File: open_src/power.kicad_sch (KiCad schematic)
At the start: 9 parts

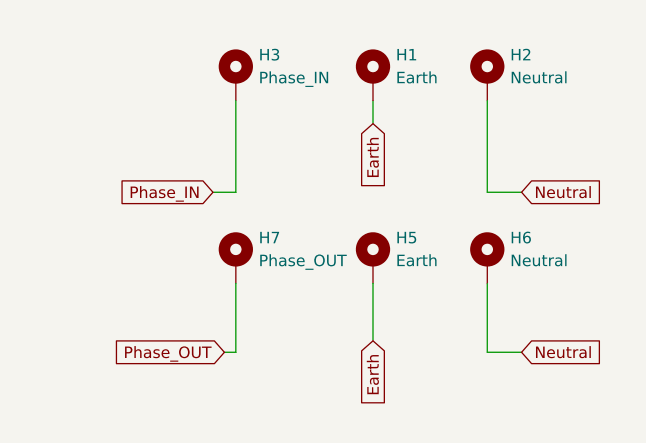
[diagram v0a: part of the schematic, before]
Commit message: Added trace
Still not yet cross checked
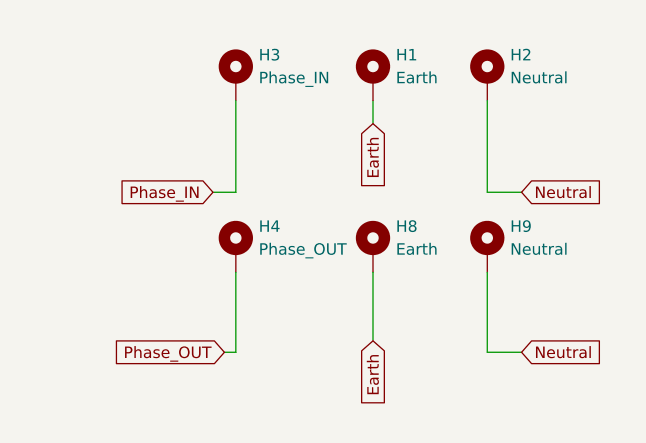
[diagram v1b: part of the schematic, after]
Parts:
- removed H5: Earth, Mounting_Wuerth:Mounting_Wuerth_WA-SMSE-ExternalM3_H8mm_9771080360, symbol Mechanical:MountingHole_Pad_MP
- removed H6: Neutral, Mounting_Wuerth:Mounting_Wuerth_WA-SMSE-ExternalM3_H5mm_9771050360, symbol Mechanical:MountingHole_Pad_MP
- removed H7: Phase_OUT, Mounting_Wuerth:Mounting_Wuerth_WA-SMSE-ExternalM3_H5mm_9771050360, symbol Mechanical:MountingHole_Pad_MP
- added H4: Phase_OUT, MountingHole:MountingHole_8.4mm_M8_Pad, symbol Mechanical:MountingHole_Pad
- added H8: Earth, MountingHole:MountingHole_8.4mm_M8_Pad, symbol Mechanical:MountingHole_Pad
- added H9: Neutral, MountingHole:MountingHole_8.4mm_M8_Pad, symbol Mechanical:MountingHole_Pad
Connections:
- net Earth: now also H8.1
- net Neutral: now also H9.1
- net Phase_OUT: now also H4.1
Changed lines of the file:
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@@
     (stroke (width 0) (type default))
   )
-  (wire (pts (xy 213.36 100.33) (xy 213.36 107.95))
+  (wire (pts (xy 213.36 99.06) (xy 213.36 107.95))
     (stroke (width 0) (type default))
   )
@@
     (stroke (width 0) (type default))
   )
-  (wire (pts (xy 228.6 100.33) (xy 228.6 106.68))
+  (wire (pts (xy 228.6 99.06) (xy 228.6 106.68))
     (stroke (width 0) (type default))
   )
@@
     (stroke (width 0) (type default))
   )
-  (wire (pts (xy 241.3 100.33) (xy 241.3 107.95))
+  (wire (pts (xy 241.3 99.06) (xy 241.3 107.95))
     (stroke (width 0) (type default))
   )
@@
     )
   )
+  (symbol (lib_id "Mechanical:MountingHole_Pad") (at 213.36 96.52 0) (unit 1)
+    (in_bom yes) (on_board yes) (dnp no) (fields_autoplaced)
+    (property "Reference" "H4" (at 215.9 93.98 0)
+      (effects (font (size 1.27 1.27)) (justify left))
+    )
+    (property "Value" "Phase_OUT" (at 215.9 96.52 0)
+      (effects (font (size 1.27 1.27)) (justify left))
+    )
+    (property "Footprint" "MountingHole:MountingHole_8.4mm_M8_Pad" (at 213.36 96.52 0)
+      (effects (font (size 1.27 1.27)) hide)
+    )
+    (property "Datasheet" "~" (at 213.36 96.52 0)
+      (effects (font (size 1.27 1.27)) hide)
+    )
+    (pin "1")
+    (instances
+      (project "open_src"
+        (path "/0eec0a72-c8ab-4737-8598-de474fd425a5/a922efa4-6ed1-4252-b0de-28fa44c32c4a"
+          (reference "H4") (unit 1)
+        )
+      )
+    )
+  )
+  (symbol (lib_id "Mechanical:MountingHole_Pad") (at 228.6 96.52 0) (unit 1)
+    (in_bom yes) (on_board yes) (dnp no) (fields_autoplaced)
+    (property "Reference" "H8" (at 231.14 93.98 0)
+      (effects (font (size 1.27 1.27)) (justify left))
+    )
+    (property "Value" "Earth" (at 231.14 96.52 0)
+      (effects (font (size 1.27 1.27)) (justify left))
+    )
+    (property "Footprint" "MountingHole:MountingHole_8.4mm_M8_Pad" (at 228.6 96.52 0)
+      (effects (font (size 1.27 1.27)) hide)
+    )
+    (property "Datasheet" "~" (at 228.6 96.52 0)
+      (effects (font (size 1.27 1.27)) hide)
+    )
+    (pin "1")
+    (instances
+      (project "open_src"
+        (path "/0eec0a72-c8ab-4737-8598-de474fd425a5/a922efa4-6ed1-4252-b0de-28fa44c32c4a"
+          (reference "H8") (unit 1)
+        )
+      )
+    )
+  )
   (symbol (lib_id "2024-01-15_18-52-43:B72214S0271K101") (at 91.44 104.14 90) (unit 1)
     (in_bom yes) (on_board yes) (dnp no) (fields_autoplaced)
@@
     )
   )
-  (symbol (lib_id "Mechanical:MountingHole_Pad_MP") (at 213.36 97.79 0) (unit 1)
-    (in_bom yes) (on_board yes) (dnp no) (fields_autoplaced)
-    (property "Reference" "H7" (at 215.9 95.25 0)
-      (effects (font (size 1.27 1.27)) (justify left))
-    )
-    (property "Value" "Phase_OUT" (at 215.9 97.79 0)
-      (effects (font (size 1.27 1.27)) (justify left))
-    )
-    (property "Footprint" "Mounting_Wuerth:Mounting_Wuerth_WA-SMSE-ExternalM3_H5mm_9771050360" (at 213.36 97.79 0)
-      (effects (font (size 1.27 1.27)) hide)
-    )
-    (property "Datasheet" "~" (at 213.36 97.79 0)
-      (effects (font (size 1.27 1.27)) hide)
-    )
-    (pin "MP")
-    (instances
-      (project "open_src"
-        (path "/0eec0a72-c8ab-4737-8598-de474fd425a5/a922efa4-6ed1-4252-b0de-28fa44c32c4a"
-          (reference "H7") (unit 1)
-        )
-      )
-    )
-  )
-  (symbol (lib_id "Mechanical:MountingHole_Pad_MP") (at 241.3 97.79 0) (unit 1)
-    (in_bom yes) (on_board yes) (dnp no) (fields_autoplaced)
-    (property "Reference" "H6" (at 243.84 95.25 0)
-      (effects (font (size 1.27 1.27)) (justify left))
-    )
-    (property "Value" "Neutral" (at 243.84 97.79 0)
-      (effects (font (size 1.27 1.27)) (justify left))
-    )
-    (property "Footprint" "Mounting_Wuerth:Mounting_Wuerth_WA-SMSE-ExternalM3_H5mm_9771050360" (at 241.3 97.79 0)
-      (effects (font (size 1.27 1.27)) hide)
-    )
-    (property "Datasheet" "~" (at 241.3 97.79 0)
-      (effects (font (size 1.27 1.27)) hide)
-    )
-    (pin "MP")
-    (instances
-      (project "open_src"
-        (path "/0eec0a72-c8ab-4737-8598-de474fd425a5/a922efa4-6ed1-4252-b0de-28fa44c32c4a"
-          (reference "H6") (unit 1)
-        )
-      )
-    )
-  )
   (symbol (lib_id "Mechanical:MountingHole_Pad") (at 241.3 77.47 0) (unit 1)
     (in_bom yes) (on_board yes) (dnp no) (fields_autoplaced)
@@
     )
   )
+  (symbol (lib_id "Mechanical:MountingHole_Pad") (at 241.3 96.52 0) (unit 1)
+    (in_bom yes) (on_board yes) (dnp no) (fields_autoplaced)
+    (property "Reference" "H9" (at 243.84 93.98 0)
+      (effects (font (size 1.27 1.27)) (justify left))
+    )
+    (property "Value" "Neutral" (at 243.84 96.52 0)
+      (effects (font (size 1.27 1.27)) (justify left))
+    )
+    (property "Footprint" "MountingHole:MountingHole_8.4mm_M8_Pad" (at 241.3 96.52 0)
+      (effects (font (size 1.27 1.27)) hide)
+    )
+    (property "Datasheet" "~" (at 241.3 96.52 0)
+      (effects (font (size 1.27 1.27)) hide)
+    )
+    (pin "1")
+    (instances
+      (project "open_src"
+        (path "/0eec0a72-c8ab-4737-8598-de474fd425a5/a922efa4-6ed1-4252-b0de-28fa44c32c4a"
+          (reference "H9") (unit 1)
+        )
+      )
+    )
+  )
   (symbol (lib_id "power:GND") (at 163.83 100.33 0) (unit 1)
     (in_bom yes) (on_board yes) (dnp no) (fields_autoplaced)
@@
         )
       )
-    )
-  )
-  (symbol (lib_id "Mechanical:MountingHole_Pad_MP") (at 228.6 97.79 0) (unit 1)
-    (in_bom yes) (on_board yes) (dnp no) (fields_autoplaced)
-    (property "Reference" "H5" (at 231.14 95.25 0)
-      (effects (font (size 1.27 1.27)) (justify left))
-    )
-    (property "Value" "Earth" (at 231.14 97.79 0)
-      (effects (font (size 1.27 1.27)) (justify left))
-    )
-    (property "Footprint" "Mounting_Wuerth:Mounting_Wuerth_WA-SMSE-ExternalM3_H8mm_9771080360" (at 228.6 97.79 0)
-      (effects (font (size 1.27 1.27)) hide)
-    )
-    (property "Datasheet" "~" (at 228.6 97.79 0)
-      (effects (font (size 1.27 1.27)) hide)
-    )
-    (pin "MP")
-    (instances
-      (project "open_src"
-        (path "/0eec0a72-c8ab-4737-8598-de474fd425a5/a922efa4-6ed1-4252-b0de-28fa44c32c4a"
-          (reference "H5") (unit 1)
-        )
-      )
